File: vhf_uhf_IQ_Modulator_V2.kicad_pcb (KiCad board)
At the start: 2 copper layers, 71 parts, among them J1 CONN_01X03, J2 TEST_1P, J3 Audio-Jack-3, J4 CONN_01X04, J5 SMA Edge FM, Q1 BC817-40, Q2 BC817-40, Q3 BC817-40, U1 TRF3701, U2 MMZ09332BT1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

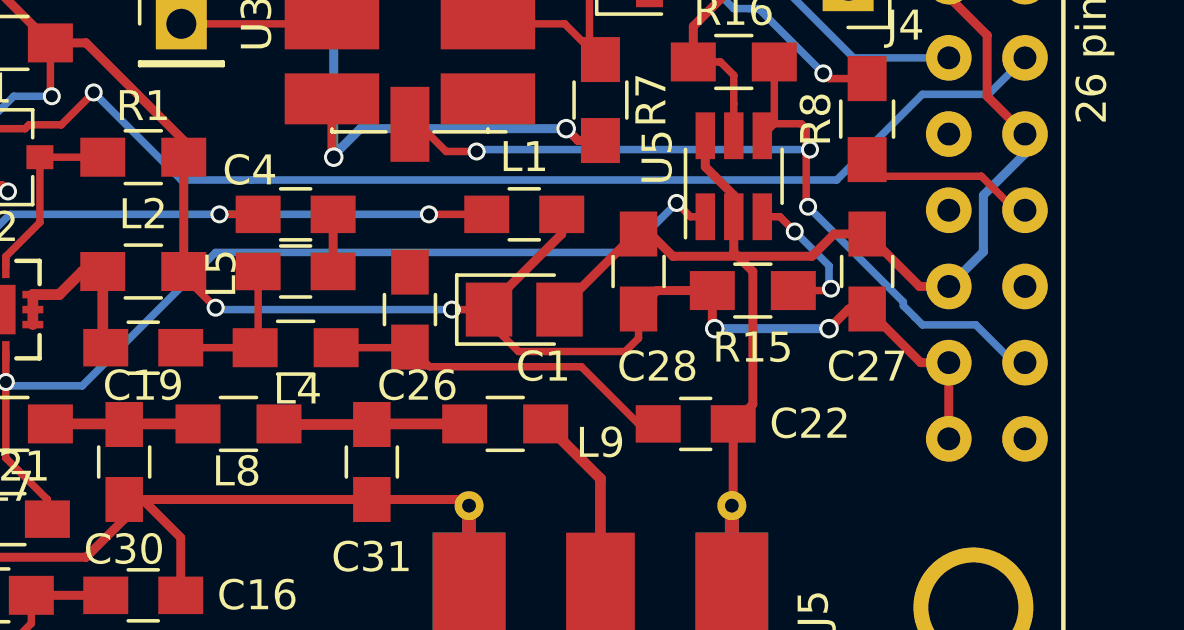
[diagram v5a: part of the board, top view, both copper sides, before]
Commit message: 19 tracks left
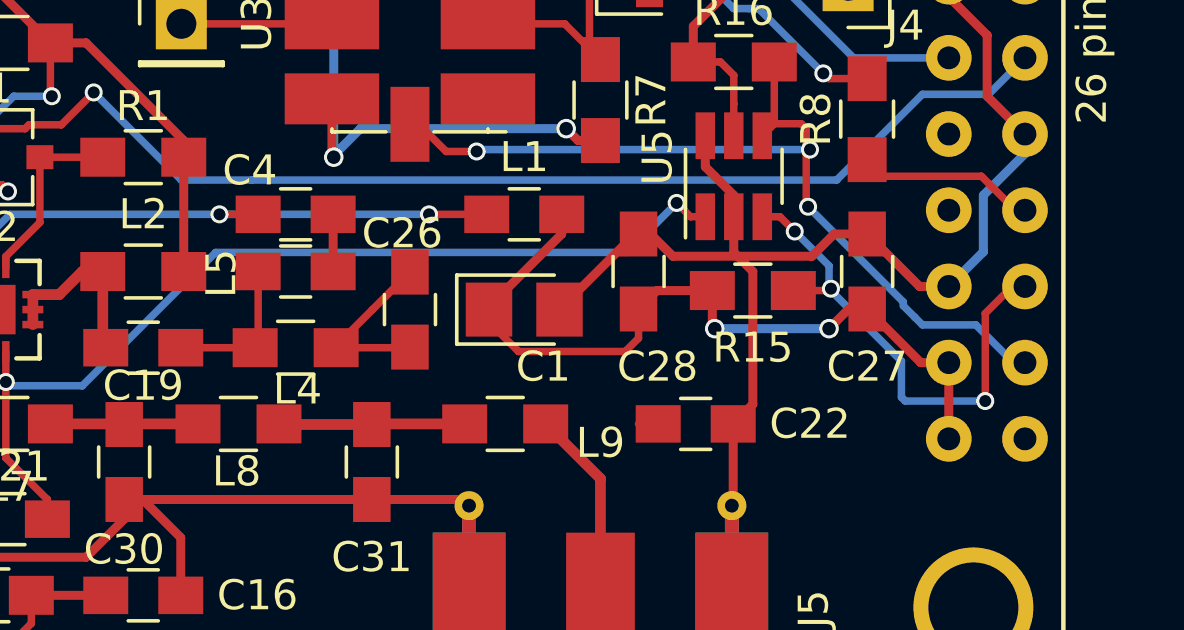
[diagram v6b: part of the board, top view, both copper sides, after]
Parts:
- turned C26 to 90 degrees
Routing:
- net SLC: track 4.97 -> 17.0 mm, vias 2 -> 3
- net +5V: track 183.6 -> 173.0 mm, vias 11 -> 9
- net Net-(C22-Pad2): track 11.8 -> 6.63 mm
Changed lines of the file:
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@@
   (general
     (links 163)
-    (no_connects 18)
+    (no_connects 19)
     (area 148.0511 54.021666 194.776101 114.845001)
     (thickness 1.6)
     (drawings 0)
-    (tracks 534)
+    (tracks 537)
     (zones 0)
     (modules 71)
@@
     (visible_elements FFFEFFFF)
     (pcbplotparams
-      (layerselection 0x00030_80000001)
+      (layerselection 0x3ffff_80000001)
       (usegerberextensions false)
       (excludeedgelayer true)
@@
       (padsonsilk false)
       (subtractmaskfromsilk false)
-      (outputformat 1)
+      (outputformat 4)
       (mirror false)
-      (drillshape 1)
+      (drillshape 0)
       (scaleselection 1)
-      (outputdirectory ""))
+      (outputdirectory doc/))
   )
   (net 0 "")
@@
   )
   (module Capacitors_SMD:C_0805_HandSoldering (layer F.Cu)
-    (at 172.72 92.075 270)
+    (at 172.72 92.075 90)
     (descr "Capacitor SMD 0805, hand soldering")
     (tags "capacitor 0805")
     (attr smd)
-    (fp_text reference C26 (at 2.54 -0.254 360) (layer F.SilkS)
+    (fp_text reference C26 (at 2.54 -0.254 180) (layer F.SilkS)
       (effects (font (size 1 1) (thickness 0.15)))
     )
-    (fp_text value 220pF (at 0 1.75 270) (layer F.Fab)
+    (fp_text value 220pF (at 0 1.75 90) (layer F.Fab)
       (effects (font (size 1 1) (thickness 0.15)))
     )
-    (fp_text user %R (at 2.54 -0.254 360) (layer F.Fab)
+    (fp_text user %R (at 2.54 -0.254 180) (layer F.Fab)
       (effects (font (size 1 1) (thickness 0.15)))
     )
@@
     (fp_line (start 2.25 0.87) (end 2.25 -0.88) (layer F.CrtYd) (width 0.05))
     (fp_line (start 2.25 0.87) (end -2.25 0.87) (layer F.CrtYd) (width 0.05))
-    (pad 1 smd rect (at -1.25 0 270) (size 1.5 1.25) (layers F.Cu F.Paste F.Mask)
+    (pad 1 smd rect (at -1.25 0 90) (size 1.5 1.25) (layers F.Cu F.Paste F.Mask)
       (net 23 "Net-(C26-Pad1)"))
-    (pad 2 smd rect (at 1.25 0 270) (size 1.5 1.25) (layers F.Cu F.Paste F.Mask)
+    (pad 2 smd rect (at 1.25 0 90) (size 1.5 1.25) (layers F.Cu F.Paste F.Mask)
       (net 17 "Net-(C22-Pad2)"))
     (model Capacitors_SMD.3dshapes/C_0805.wrl
@@
   )
   (segment (start 165.18 90.805) (end 165.18 90.9485) (width 0.25) (layer F.Cu) (net 1))
-  (segment (start 165.18 90.9485) (end 166.243 92.0115) (width 0.25) (layer F.Cu) (net 1))
-  (segment (start 174.117 92.075) (end 175.355 92.075) (width 0.25) (layer F.Cu) (net 1))
-  (via (at 174.117 92.075) (size 0.6) (drill 0.4) (layers F.Cu B.Cu) (net 1))
-  (segment (start 166.3065 92.075) (end 174.117 92.075) (width 0.25) (layer B.Cu) (net 1))
-  (segment (start 166.243 92.0115) (end 166.3065 92.075) (width 0.25) (layer B.Cu) (net 1))
-  (via (at 166.243 92.0115) (size 0.6) (drill 0.4) (layers F.Cu B.Cu) (net 1))
   (segment (start 175.355 92.075) (end 175.355 92.4875) (width 0.25) (layer F.Cu) (net 1))
   (segment (start 175.355 92.4875) (end 176.3395 93.472) (width 0.25) (layer F.Cu) (net 1))
@@
   (segment (start 159.25 97.02) (end 160.635 98.405) (width 0.25) (layer F.Cu) (net 16))
   (segment (start 180.995 95.885) (end 180.34 95.885) (width 0.25) (layer F.Cu) (net 17))
-  (segment (start 180.34 95.885) (end 178.435 93.98) (width 0.25) (layer F.Cu) (net 17))
-  (segment (start 178.435 93.98) (end 173.375 93.98) (width 0.25) (layer F.Cu) (net 17))
-  (segment (start 173.375 93.98) (end 172.72 93.325) (width 0.25) (layer F.Cu) (net 17))
+  (segment (start 170.26 93.345) (end 170.26 93.285) (width 0.25) (layer F.Cu) (net 17))
+  (segment (start 170.26 93.285) (end 171.47 92.075) (width 0.25) (layer F.Cu) (net 17))
+  (segment (start 171.47 92.075) (end 172.72 90.825) (width 0.25) (layer F.Cu) (net 17))
   (segment (start 170.26 93.345) (end 172.7 93.345) (width 0.25) (layer F.Cu) (net 17))
-  (segment (start 172.7 93.345) (end 172.72 93.325) (width 0.25) (layer F.Cu) (net 17))
   (segment (start 155.555 86.36) (end 155.575 86.36) (width 0.25) (layer F.Cu) (net 18))
   (segment (start 155.575 86.36) (end 156.845 85.09) (width 0.25) (layer F.Cu) (net 18))
@@
   (segment (start 153.035 83.82) (end 153.055 83.82) (width 0.25) (layer F.Cu) (net 22))
   (segment (start 150.0411 93.8436) (end 150.0411 93.7989) (width 0.25) (layer F.Cu) (net 22))
+  (segment (start 172.7 93.345) (end 172.72 93.325) (width 0.25) (layer F.Cu) (net 23))
   (segment (start 158.035 95.885) (end 155.595 95.885) (width 0.36) (layer F.Cu) (net 24))
   (segment (start 155.595 95.885) (end 154.88 96.6) (width 0.36) (layer F.Cu) (net 24))
@@
   (via (at 182.245 78.4225) (size 0.6) (drill 0.4) (layers F.Cu B.Cu) (net 43))
   (segment (start 187.5061 83.6836) (end 182.245 78.4225) (width 0.25) (layer B.Cu) (net 43))
+  (segment (start 186.7535 91.3765) (end 186.7535 91.44) (width 0.25) (layer B.Cu) (net 44))
+  (segment (start 191.897 92.202) (end 192.7954 91.3036) (width 0.25) (layer F.Cu) (net 44) (status 800000))
+  (segment (start 191.897 95.123) (end 191.897 92.202) (width 0.25) (layer F.Cu) (net 44))
+  (via (at 191.897 95.123) (size 0.6) (drill 0.4) (layers F.Cu B.Cu) (net 44))
+  (segment (start 189.23 95.123) (end 191.897 95.123) (width 0.25) (layer B.Cu) (net 44))
+  (segment (start 189.103 94.996) (end 189.23 95.123) (width 0.25) (layer B.Cu) (net 44))
+  (segment (start 189.103 93.7895) (end 189.103 94.996) (width 0.25) (layer B.Cu) (net 44))
+  (segment (start 186.7535 91.44) (end 189.103 93.7895) (width 0.25) (layer B.Cu) (net 44))
+  (segment (start 192.7954 91.3036) (end 193.2211 91.3036) (width 0.25) (layer F.Cu) (net 44) (status C00000))
   (segment (start 185.5 91.44) (end 186.69 91.44) (width 0.25) (layer F.Cu) (net 44))
   (segment (start 185.0555 88.98) (end 184.465 88.98) (width 0.25) (layer F.Cu) (net 44))
@@
   (via (at 186.7535 91.3765) (size 0.6) (drill 0.4) (layers F.Cu B.Cu) (net 44))
   (segment (start 186.69 91.44) (end 186.7535 91.3765) (width 0.25) (layer F.Cu) (net 44))
-  (segment (start 172.72 85.9) (end 173.022 85.9) (width 0.25) (layer F.Cu) (net 45) (status C00000))
-  (segment (start 173.022 85.9) (end 173.9265 86.8045) (width 0.25) (layer F.Cu) (net 45) (status 400000))
+  (segment (start 172.72 85.9) (end 173.022 85.9) (width 0.25) (layer F.Cu) (net 45))
+  (segment (start 173.022 85.9) (end 173.9265 86.8045) (width 0.25) (layer F.Cu) (net 45))
   (segment (start 173.9265 86.8045) (end 174.9425 86.8045) (width 0.25) (layer F.Cu) (net 45))
   (via (at 174.9425 86.8045) (size 0.6) (drill 0.4) (layers F.Cu B.Cu) (net 45))
